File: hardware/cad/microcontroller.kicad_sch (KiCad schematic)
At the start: 48 parts, among them J401 6-440054-2, J402 6-440129-2, J403 2x2 PIN HEADER, J404 6-440054-2, J405 6-440129-2, J406 6-440054-2, J407 6-440129-2, J408 6-440054-2, J409 6-440129-2, Q401 DMN2050, Q402 DMN2050, SW401 FOOTSWITCH, SW402 FOOTSWITCH, U401 STM32G031K8U6

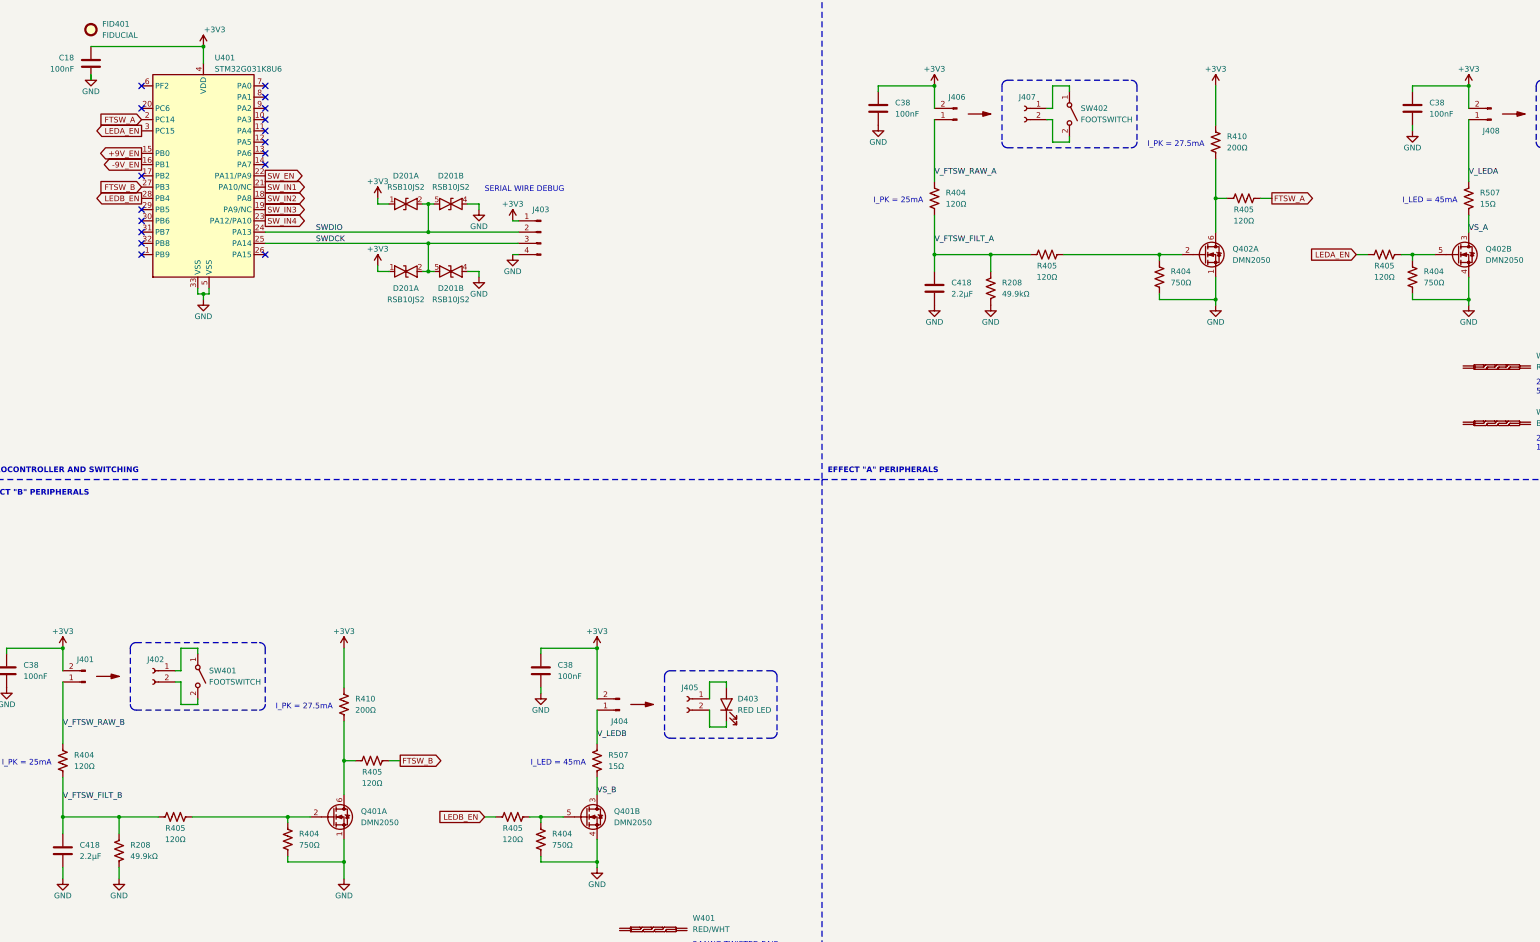
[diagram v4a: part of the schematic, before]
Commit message: board layout first pass
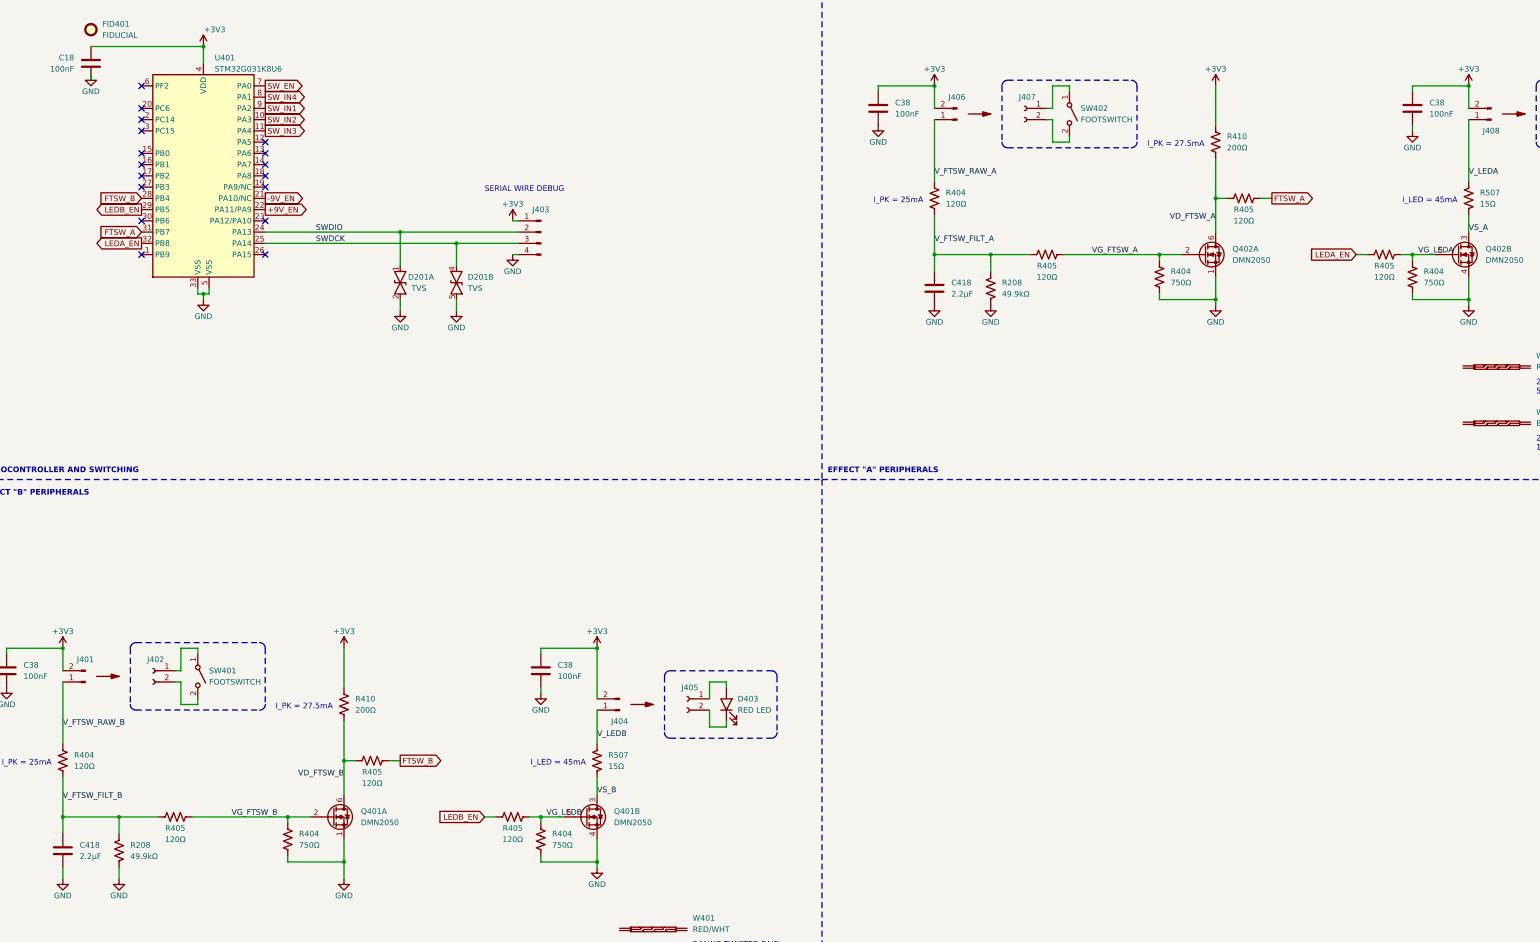
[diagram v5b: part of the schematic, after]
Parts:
- removed D201 (x2): RSB10JS2, Library:RSB12JS2, symbol Library:ROHM_RSB12JS2
- added D201: TVS, Library:RSB12JS2, symbol Library:ROHM_RSB12JS2
- C418: value 2.2µF -> 2.2μF
- R410: footprint Resistor_SMD:R_0603_1608Metric -> Resistor_SMD:R_0402_1005Metric
- U401: footprint Library:QFN-32-1EP_5x5mm_P0.5mm_EP3.45x3.45mm -> Package_DFN_QFN:QFN-32-1EP_5x5mm_P0.5mm_EP3.45x3.45mm_ThermalVias
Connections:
- net +9V_EN: now also U401.22 (PA11/PA9); no longer U401.15 (PB0)
- net -9V_EN: now also U401.21 (PA10/NC); no longer U401.16 (PB1)
- net FTSW_A: now also U401.31 (PB7); no longer U401.2 (PC14)
- net FTSW_B: now also U401.28 (PB4); no longer U401.27 (PB3)
- net GND: now also D201.2, D201.5
- net LEDA_EN: now also U401.32 (PB8); no longer U401.3 (PC15)
- net LEDB_EN: now also U401.29 (PB5); no longer U401.28 (PB4)
- net SWDCK: now also D201.4
- net SWDIO: now also D201.1
- net SW_EN: now also U401.7 (PA0); no longer U401.22 (PA11/PA9)
- net SW_IN1: now also U401.9 (PA2); no longer U401.21 (PA10/NC)
- net SW_IN2: now also U401.10 (PA3); no longer U401.18 (PA8)
- net SW_IN3: now also U401.11 (PA4); no longer U401.19 (PA9/NC)
- net SW_IN4: now also U401.8 (PA1); no longer U401.23 (PA12/PA10)
- net VD_FTSW_B: now reaches Q401.6 (D), R405.1, R410.2
- net VG_LEDB: now reaches Q401.5 (G), R404.1, R405.2
- net VG_LEDA: now reaches Q402.5 (G), R404.1, R405.2
- net VD_FTSW_A: now reaches Q402.6 (D), R405.1, R410.2
- net VG_FTSW_A: now reaches Q402.2 (G), R404.1, R405.2
- net VG_FTSW_B: now reaches Q401.2 (G), R404.1, R405.2

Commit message: an inappropriately large commit
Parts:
- added H401, H402, H403, H404: JLC_TOOLING_HOLE, Library:JLC_Tooling_hole, symbol Mechanical:MountingHole
- C18, C38: Part Number GRM155R61H104KE19J -> GRM188C71E225KE11D
- C418: Part Number GRM188R61H225KE11J -> GRM188Z71E225KE43D
- D201: value TVS -> RSB12JS2
- R208: Part Number (none) -> RK73H1ETTP4992F
- R404, R405: Part Number (none) -> RK73H1ETTP1200F
- R404: Part Number (none) -> RK73H1ETTP7500F
- R410: Part Number (none) -> RK73H1ETTP2000F
- R507: Part Number (none) -> RK73H1JTTD15R0F
- U401: footprint Package_DFN_QFN:QFN-32-1EP_5x5mm_P0.5mm_EP3.45x3.45mm_ThermalVias -> Library:QFN-32-1EP_5x5mm_P0.5mm_EP3.45x3.45mm
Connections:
- net +9V_EN: now also U401.32 (PB8); no longer U401.22 (PA11/PA9)
- net -9V_EN: now also U401.31 (PB7); no longer U401.21 (PA10/NC)
- net FTSW_A: now also U401.9 (PA2); no longer U401.31 (PB7)
- net FTSW_B: now also U401.1 (PB9); no longer U401.28 (PB4)
- net LEDA_EN: now also U401.10 (PA3); no longer U401.32 (PB8)
- net LEDB_EN: now also U401.2 (PC14); no longer U401.29 (PB5)
- net SW_IN1: now also U401.17 (PB2); no longer U401.9 (PA2)
- net SW_IN2: now also U401.21 (PA10/NC); no longer U401.10 (PA3)
- net SW_IN3: now also U401.20 (PC6); no longer U401.11 (PA4)
- net SW_IN4: now also U401.19 (PA9/NC); no longer U401.8 (PA1)
- net ~{SW_EN}: now reaches U401.18 (PA8)
- net SW_EN: no longer names the net of U401.7 (PA0)
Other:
- note added: "MECHANICAL"
- company: ALESSANDRO RIZZONI -> Alessandro Rizzoni
- title: BASEBOARD -> Baseboard
